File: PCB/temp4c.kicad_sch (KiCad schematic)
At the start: 40 parts, among them J1 10-24VAC, J2 USB_IN, J3 eflashy32, J4 THERMO1, J5 THERMO2, J6 THERMO3, J7 THERMO4, U1 VXO7803-500, U2 ESP32-WROOM-32D, U3 SHT35-DISB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

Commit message: lcsc PN for esp32
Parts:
- U2: LCSC (none) -> C701342
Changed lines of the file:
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@@
+      (effects (font (size 1.27 1.27)) hide)
+    )
+    (property "LCSC" "C701342" (id 4) (at 49.53 67.31 0)
       (effects (font (size 1.27 1.27)) hide)
     )

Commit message: switch rectifier
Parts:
- removed D1: MB10S, Diode_SMD:Diode_Bridge_DiodesInc_MBS, symbol Device:D_Bridge_+-AA
- removed D2: SS14, Diode_SMD:D_SMA, symbol Device:D_Schottky
- added D1, D2, D3, D4, D5: B5819, Diode_SMD:D_SOD-123, symbol Device:D_Schottky_Small
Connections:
- net 5VUSB: now also D2.1 (K)
- net GND: now also D1.2 (A), D4.2 (A)
- net at C2.1, C3.1, C4.1: now also D2.2 (A), D3.1 (K), D5.1 (K)
- net at F1.1: now also D1.1 (K), D3.2 (A)
- net at J1.1 (Pin_1): now also D4.1 (K), D5.2 (A)
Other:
- moved on the sheet: F1, J1

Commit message: Tidy/labels
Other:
- note added: "ESP32"
- note added: "Onboard Temp/Humidity"
- note added: "Power"
- note added: "Thermocouples"
- moved on the sheet: C1, C10, C11, C12, C13, C14, C15, C16, C2, C3, C4, C5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

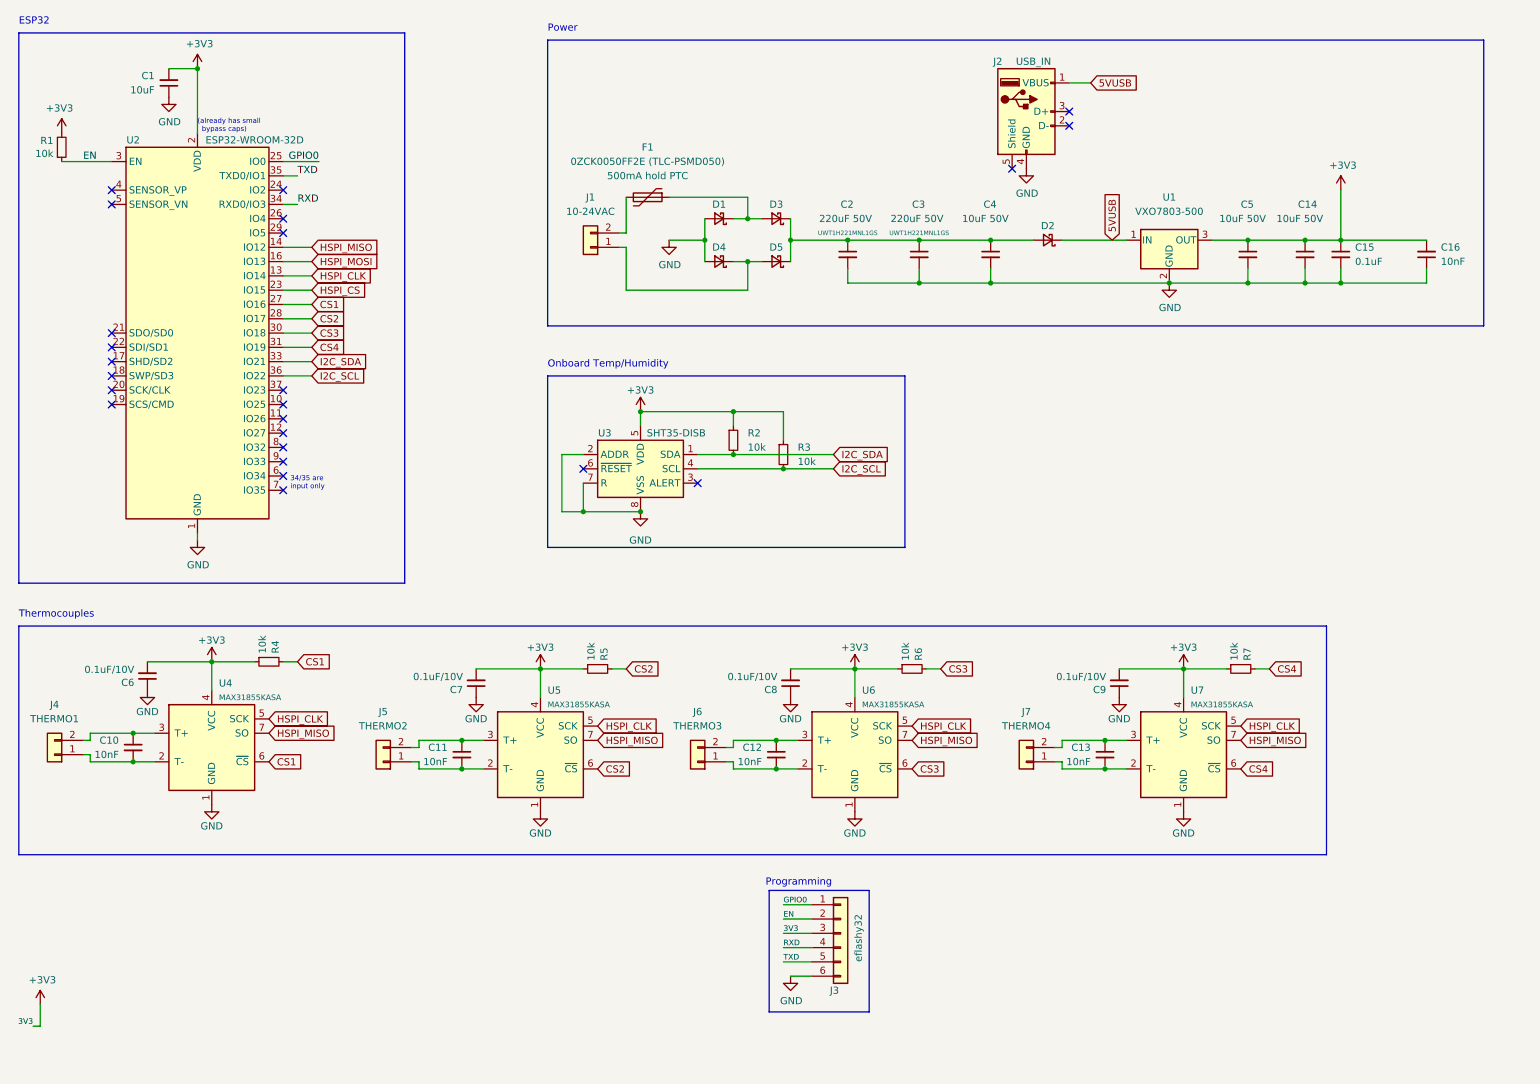
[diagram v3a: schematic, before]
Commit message: esptemp8c rename
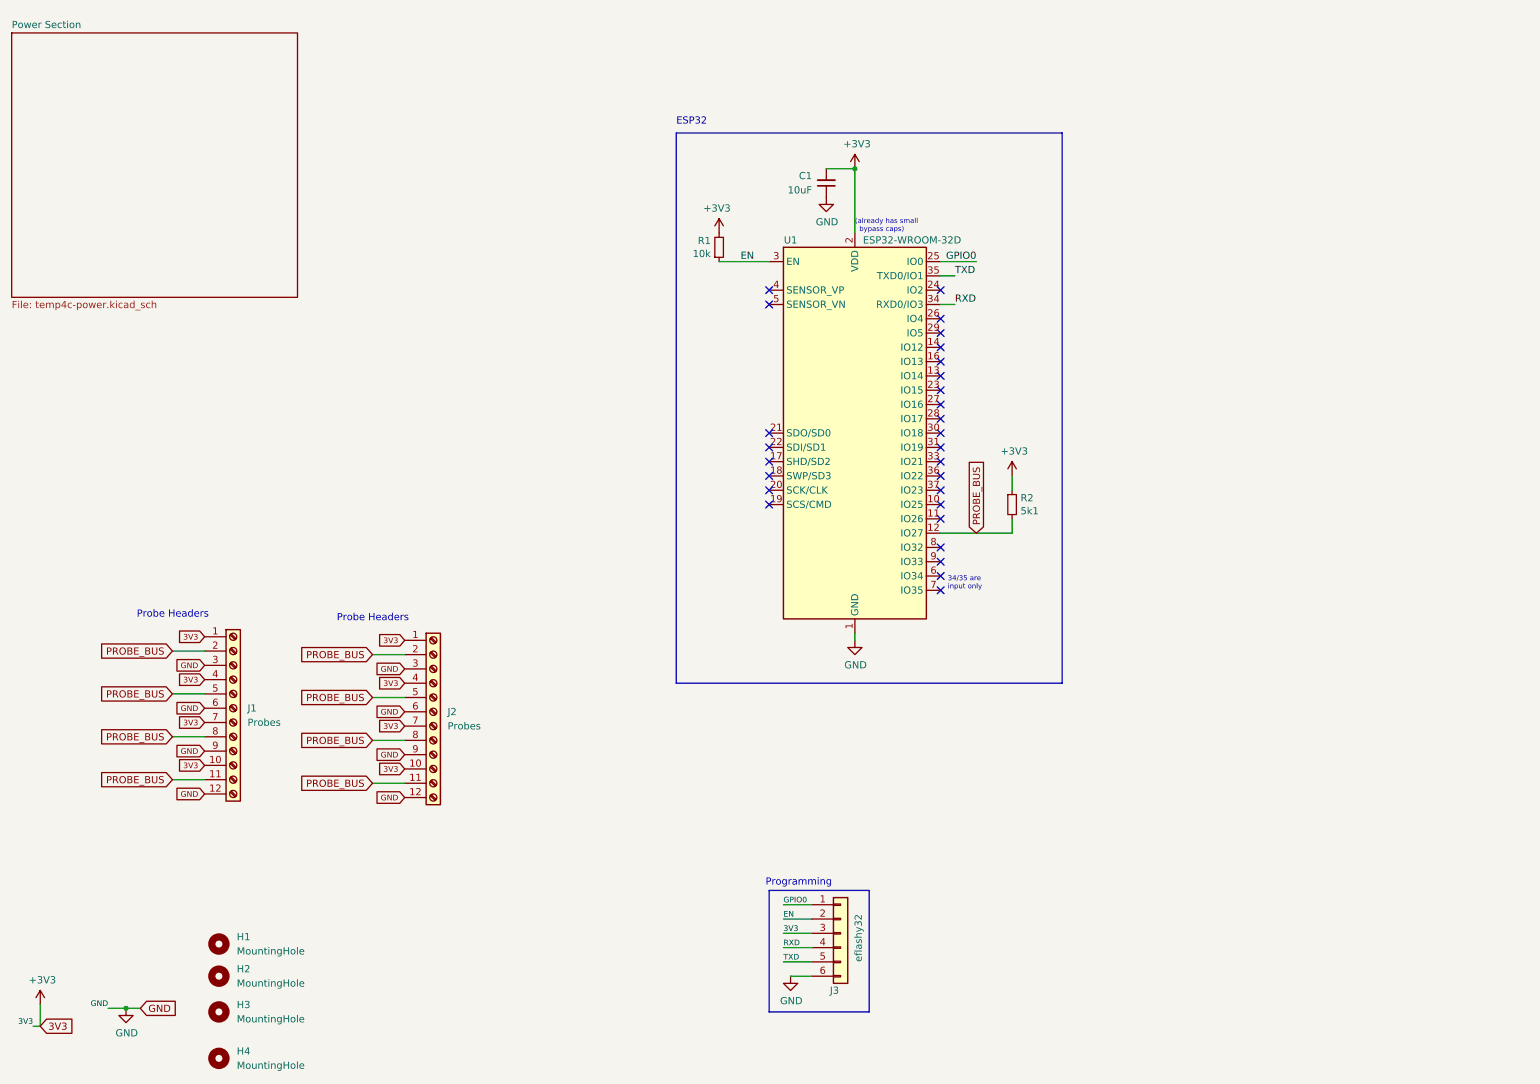
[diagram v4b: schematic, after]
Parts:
- removed C10, C11, C12, C13, C16: 10nF, Capacitor_SMD:C_0402_1005Metric, symbol Device:C_Small
- removed C14, C4, C5: 10uF 50V, Capacitor_SMD:C_1206_3216Metric, symbol Device:C_Small
- removed C15: 0.1uF, Capacitor_SMD:C_0805_2012Metric, symbol Device:C_Small
- removed C2, C3: 220uF 50V, Capacitor_SMD:CP_Elec_10x10, symbol Device:C_Small
- removed C6, C7, C8, C9: 0.1uF/10V, Capacitor_SMD:C_0805_2012Metric, symbol Device:C_Small
- removed D1, D2, D3, D4, D5: B5819, Diode_SMD:D_SOD-123, symbol Device:D_Schottky_Small
- removed F1: 0ZCK0050FF2E (TLC-PSMD050), Fuse:Fuse_0805_2012Metric_Pad1.15x1.40mm_HandSolder, symbol Device:Polyfuse
- removed J1: 10-24VAC, Connector_Phoenix_MC:PhoenixContact_MC_1,5_2-G-3.81_1x02_P3.81mm_Horizontal, symbol Connector_Generic:Conn_01x02
- removed J2: USB_IN, Connector_USB:USB_Micro-B_Amphenol_10118194_Horizontal, symbol Connector:USB_A
- removed J4: THERMO1, Connector_Phoenix_MC:PhoenixContact_MC_1,5_2-G-3.81_1x02_P3.81mm_Horizontal, symbol Connector_Generic:Conn_01x02
- removed J5: THERMO2, Connector_Phoenix_MC:PhoenixContact_MC_1,5_2-G-3.81_1x02_P3.81mm_Horizontal, symbol Connector_Generic:Conn_01x02
- removed J6: THERMO3, Connector_Phoenix_MC:PhoenixContact_MC_1,5_2-G-3.81_1x02_P3.81mm_Horizontal, symbol Connector_Generic:Conn_01x02
- removed J7: THERMO4, Connector_Phoenix_MC:PhoenixContact_MC_1,5_2-G-3.81_1x02_P3.81mm_Horizontal, symbol Connector_Generic:Conn_01x02
- removed R3: 10k, Resistor_SMD:R_0805_2012Metric, symbol Device:R_Small
- removed R4, R5, R6, R7: 10k, Resistor_SMD:R_1206_3216Metric, symbol Device:R_Small
- removed U1: VXO7803-500, temp4c:CUI-VXO7803-500, symbol Regulator_Linear:L7805
- removed U3: SHT35-DISB, Sensor_Humidity:Sensirion_DFN-8-1EP_2.5x2.5mm_P0.5mm_EP1.1x1.7mm, symbol Sensor_Humidity:SHT30-DIS
- removed U4, U5, U6, U7: MAX31855KASA, Package_SO:SOIC-8_3.9x4.9mm_P1.27mm, symbol Sensor_Temperature:MAX31855KASA
- added H1, H2, H3, H4: MountingHole, MountingHole:MountingHole_3.2mm_M3, symbol Mechanical:MountingHole
- added J1, J2: Probes, TerminalBlock_Phoenix:TerminalBlock_Phoenix_MPT-0,5-12-2.54_1x12_P2.54mm_Horizontal, symbol Connector:Screw_Terminal_01x12
- J3: LCSC (none) -> DNP
- R1: footprint Resistor_SMD:R_1206_3216Metric -> Resistor_SMD:R_0402_1005Metric; LCSC C17414 -> C25744
- R2: value 10k -> 5k1; footprint Resistor_SMD:R_0805_2012Metric -> Resistor_SMD:R_0402_1005Metric; LCSC C17414 -> C25905
- renumbered U2 to U1
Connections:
- net +3V3: now also J1.1 (Pin_1), J1.10 (Pin_10), J1.4 (Pin_4), J1.7 (Pin_7), J2.1 (Pin_1), J2.10 (Pin_10), J2.4 (Pin_4), J2.7 (Pin_7)
- net GND: now also J1.12 (Pin_12), J1.3 (Pin_3), J1.6 (Pin_6), J1.9 (Pin_9), J2.12 (Pin_12), J2.3 (Pin_3), J2.6 (Pin_6), J2.9 (Pin_9)
- net PROBE_BUS: now reaches U1.12 (IO27)
- net PROBE_BUS: now also R2.2, J1.11 (Pin_11), J1.2 (Pin_2), J1.5 (Pin_5), J1.8 (Pin_8), J2.11 (Pin_11), J2.2 (Pin_2), J2.5 (Pin_5), J2.8 (Pin_8)
- net CS1: no longer names the net of U1.27 (IO16)
- net CS2: no longer names the net of U1.28 (IO17)
- net CS3: no longer names the net of U1.30 (IO18)
- net CS4: no longer names the net of U1.31 (IO19)
- net HSPI_CLK: no longer names the net of U1.13 (IO14)
- net HSPI_CS: no longer names the net of U1.23 (IO15)
- net HSPI_MISO: no longer names the net of U1.14 (IO12)
- net HSPI_MOSI: no longer names the net of U1.16 (IO13)
- net I2C_SCL: no longer names the net of U1.36 (IO22)
- net I2C_SDA: no longer names the net of U1.33 (IO21)
- net I2C_SDA: no longer R2.2
- no-connect marks 24 -> 28
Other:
- added sheet Power Section (temp4c-power.kicad_sch)
- note added: "Probe Headers"
- note removed: "Onboard Temp/Humidity"
- note removed: "Power"
- note removed: "Thermocouples"
- moved on the sheet: C1, R1, U1

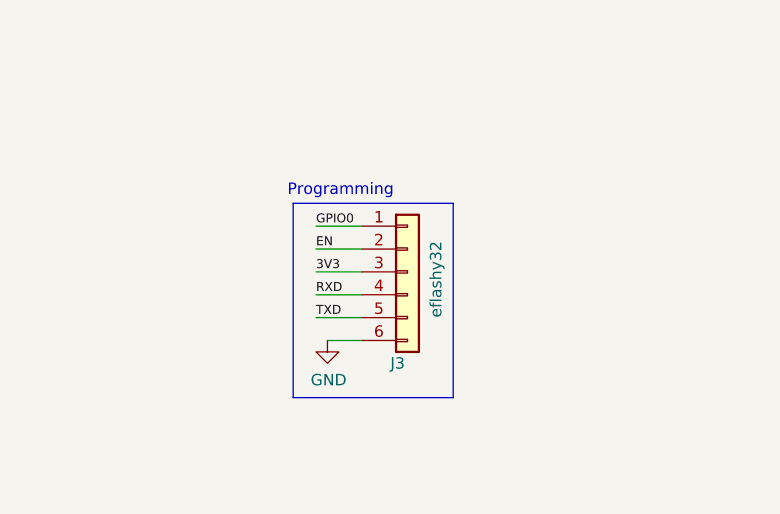
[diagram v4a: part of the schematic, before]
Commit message: fix ground pin on eflashy32
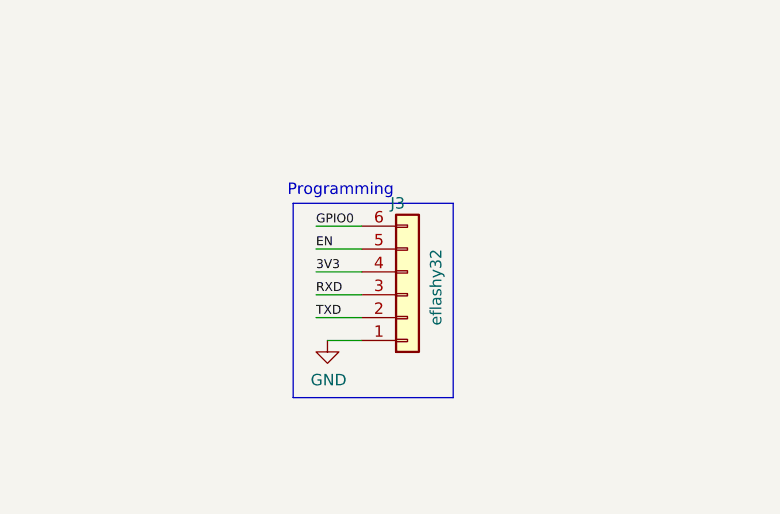
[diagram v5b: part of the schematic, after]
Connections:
- net +3V3: now also J3.4 (Pin_4); no longer J3.3 (Pin_3)
- net EN: now also J3.5 (Pin_5); no longer J3.2 (Pin_2)
- net GND: now also J3.1 (Pin_1); no longer J3.6 (Pin_6)
- net GPIO0: now also J3.6 (Pin_6); no longer J3.1 (Pin_1)
- net RXD: now also J3.3 (Pin_3); no longer J3.4 (Pin_4)
- net TXD: now also J3.2 (Pin_2); no longer J3.5 (Pin_5)
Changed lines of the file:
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@@
     (pin "1")
   )
-  (symbol (lib_id "Connector_Generic:Conn_01x06") (at 162.56 176.53 0) (unit 1)
+  (symbol (lib_id "Connector_Generic:Conn_01x06") (at 162.56 179.07 0) (mirror x) (unit 1)
     (in_bom yes) (on_board yes)
-    (property "Reference" "J3" (id 0) (at 160.655 186.69 0)
+    (property "Reference" "J3" (id 0) (at 160.655 168.91 0)
       (effects (font (size 1.27 1.27)) (justify left))
     )
-    (property "Value" "eflashy32" (id 1) (at 165.735 181.61 90)
+    (property "Value" "eflashy32" (id 1) (at 165.735 173.99 90)
       (effects (font (size 1.27 1.27)) (justify left))
     )
-    (property "Footprint" "Connector_PinHeader_2.54mm:PinHeader_1x06_P2.54mm_Vertical" (id 2) (at 162.56 176.53 0)
+    (property "Footprint" "Connector_PinHeader_2.54mm:PinHeader_1x06_P2.54mm_Vertical" (id 2) (at 162.56 179.07 0)
       (effects (font (size 1.27 1.27)) hide)
     )
-    (property "Datasheet" "~" (id 3) (at 162.56 176.53 0)
+    (property "Datasheet" "~" (id 3) (at 162.56 179.07 0)
       (effects (font (size 1.27 1.27)) hide)
     )
-    (property "LCSC" "DNP" (id 4) (at 162.56 176.53 0)
+    (property "LCSC" "DNP" (id 4) (at 162.56 179.07 0)
       (effects (font (size 1.27 1.27)) hide)
     )
